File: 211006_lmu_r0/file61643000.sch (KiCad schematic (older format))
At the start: 8 parts, among them J10 Conn_01x02, J8 Conn_01x02, J9 Conn_01x02, K1 G5V-2, Q38 BC817

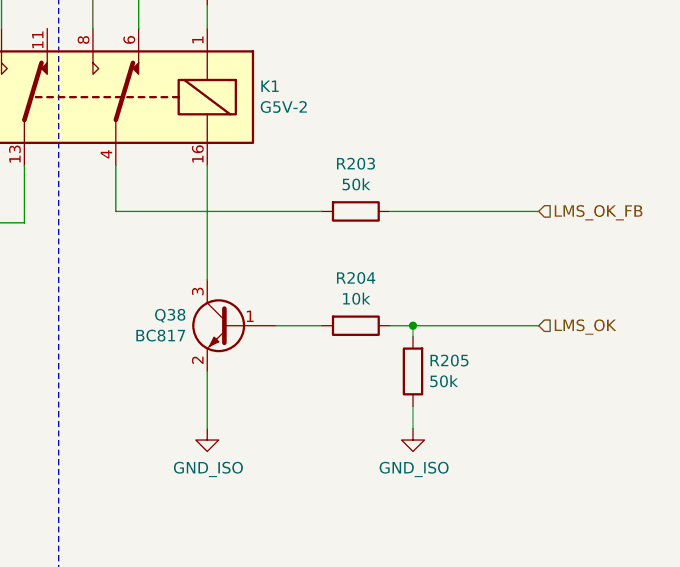
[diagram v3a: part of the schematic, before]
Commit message: Updated with Mouser links for BOM
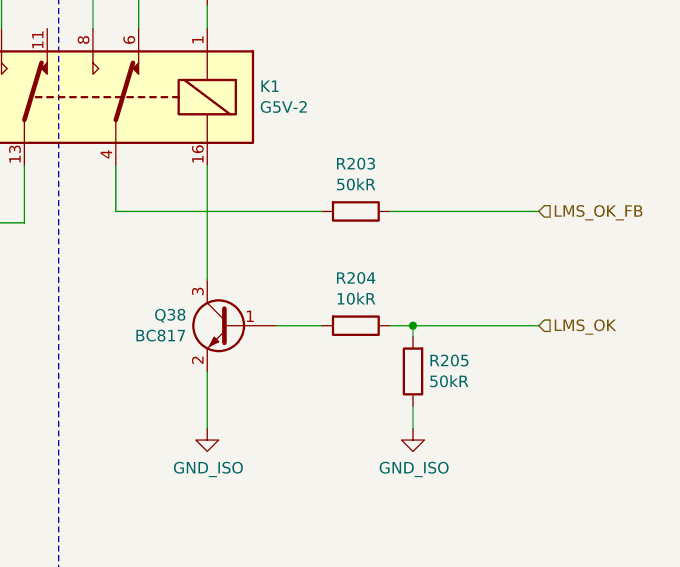
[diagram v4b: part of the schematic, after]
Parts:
- J10, J8, J9: footprint Connector_PinHeader_1.27mm:PinHeader_1x02_P1.27mm_Vertical -> Connector_PinHeader_2.54mm:PinHeader_1x02_P2.54mm_Vertical
- K1: Manufacturer (none) -> Omron; Mouser Part Number (none) -> 653-G5V-2-H1-DC12; Mouser URL (none) -> https://au.mouser.com/ProductDetail/Omron-Electronics/G5V-2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; Part Number (none) -> G5V-2-H1-DC12
- Q38: Manufacturer (none) -> Nexperia; Mouser Part Number (none) -> 771-BC817-40-T/R; Mouser URL (none) -> https://au.mouser.com/ProductDetail/Nexperia/BC817-40215?qs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; Part Number (none) -> BC817
- R203, R205: value 50k -> 50kR
- R204: value 10k -> 10kR
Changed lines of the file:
@@
 F 2 "Package_TO_SOT_SMD:SOT-23" H 6250 4125 50  0001 L CIN
 F 3 "https://www.onsemi.com/pub/Collateral/BC818-D.pdf" H 6050 4200 50  0001 L CNN
+F 4 "Nexperia" H 6050 4200 50  0001 C CNN "Manufacturer"
+F 5 "771-BC817-40-T/R" H 6050 4200 50  0001 C CNN "Mouser Part Number"
+F 6 "https://au.mouser.com/ProductDetail/Nexperia/BC817-40215?qs=sGAEpiMZZMt46bMQRT2SLrMI6Lc%252BSQ0xVQ67Chgc3gU%3D" H 6050 4200 50  0001 C CNN "Mouser URL"
+F 7 "BC817" H 6050 4200 50  0001 C CNN "Part Number"
 	1    6050 4200
 	-1   0    0    -1
@@
 P 6600 4200
 F 0 "R204" V 6393 4200 50  0000 C CNN
-F 1 "10k" V 6484 4200 50  0000 C CNN
+F 1 "10kR" V 6484 4200 50  0000 C CNN
 F 2 "Resistor_SMD:R_0603_1608Metric_Pad0.98x0.95mm_HandSolder" V 6530 4200 50  0001 C CNN
 F 3 "~" H 6600 4200 50  0001 C CNN
@@
 F 2 "Relay_THT:Relay_DPDT_Omron_G5V-2" H 6200 3150 50  0001 L CNN
 F 3 "http://omronfs.omron.com/en_US/ecb/products/pdf/en-g5v_2.pdf" H 5550 3200 50  0001 C CNN
+F 4 "Omron" H 5550 3200 50  0001 C CNN "Manufacturer"
+F 5 "653-G5V-2-H1-DC12" H 5550 3200 50  0001 C CNN "Mouser Part Number"
+F 6 "https://au.mouser.com/ProductDetail/Omron-Electronics/G5V-2-H1-DC12?qs=SXIVkn%252Bm38kUovfCr9o1Dw%3D%3D" H 5550 3200 50  0001 C CNN "Mouser URL"
+F 7 "G5V-2-H1-DC12" H 5550 3200 50  0001 C CNN "Part Number"
 	1    5550 3200
 	-1   0    0    -1
@@
 F 0 "J10" H 4568 2175 50  0000 C CNN
 F 1 "Conn_01x02" H 4568 2266 50  0000 C CNN
-F 2 "Connector_PinHeader_1.27mm:PinHeader_1x02_P1.27mm_Vertical" H 4650 2500 50  0001 C CNN
+F 2 "Connector_PinHeader_2.54mm:PinHeader_1x02_P2.54mm_Vertical" H 4650 2500 50  0001 C CNN
 F 3 "~" H 4650 2500 50  0001 C CNN
 	1    4650 2500
@@
 P 6850 4400
 F 0 "R205" H 6780 4354 50  0000 R CNN
-F 1 "50k" H 6780 4445 50  0000 R CNN
+F 1 "50kR" H 6780 4445 50  0000 R CNN
 F 2 "Resistor_SMD:R_0603_1608Metric_Pad0.98x0.95mm_HandSolder" V 6780 4400 50  0001 C CNN
 F 3 "~" H 6850 4400 50  0001 C CNN
@@
 P 6600 3700
 F 0 "R203" V 6393 3700 50  0000 C CNN
-F 1 "50k" V 6484 3700 50  0000 C CNN
+F 1 "50kR" V 6484 3700 50  0000 C CNN
 F 2 "Resistor_SMD:R_0603_1608Metric_Pad0.98x0.95mm_HandSolder" V 6530 3700 50  0001 C CNN
 F 3 "~" H 6600 3700 50  0001 C CNN
@@
 F 0 "J8" H 3918 2175 50  0000 C CNN
 F 1 "Conn_01x02" H 3918 2266 50  0000 C CNN
-F 2 "Connector_PinHeader_1.27mm:PinHeader_1x02_P1.27mm_Vertical" H 4000 2500 50  0001 C CNN
+F 2 "Connector_PinHeader_2.54mm:PinHeader_1x02_P2.54mm_Vertical" H 4000 2500 50  0001 C CNN
 F 3 "~" H 4000 2500 50  0001 C CNN
 	1    4000 2500
@@
 F 0 "J9" H 3918 2875 50  0000 C CNN
 F 1 "Conn_01x02" H 3918 2966 50  0000 C CNN
-F 2 "Connector_PinHeader_1.27mm:PinHeader_1x02_P1.27mm_Vertical" H 4000 3200 50  0001 C CNN
+F 2 "Connector_PinHeader_2.54mm:PinHeader_1x02_P2.54mm_Vertical" H 4000 3200 50  0001 C CNN
 F 3 "~" H 4000 3200 50  0001 C CNN
 	1    4000 3200
